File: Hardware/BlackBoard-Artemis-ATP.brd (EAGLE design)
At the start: 101.6 x 53.3 mm, 149 parts, among them IC3 LM1117, J2 CORTEX_DEBUG, J3 POWER_JACKTOE, J5 USB-C, Q1 1.1A/60V/600mΩ, U3 AP2112-3.3V, U4 ARTEMIS_MODULESMD, U5 CH340C, Y1 32.768kHz

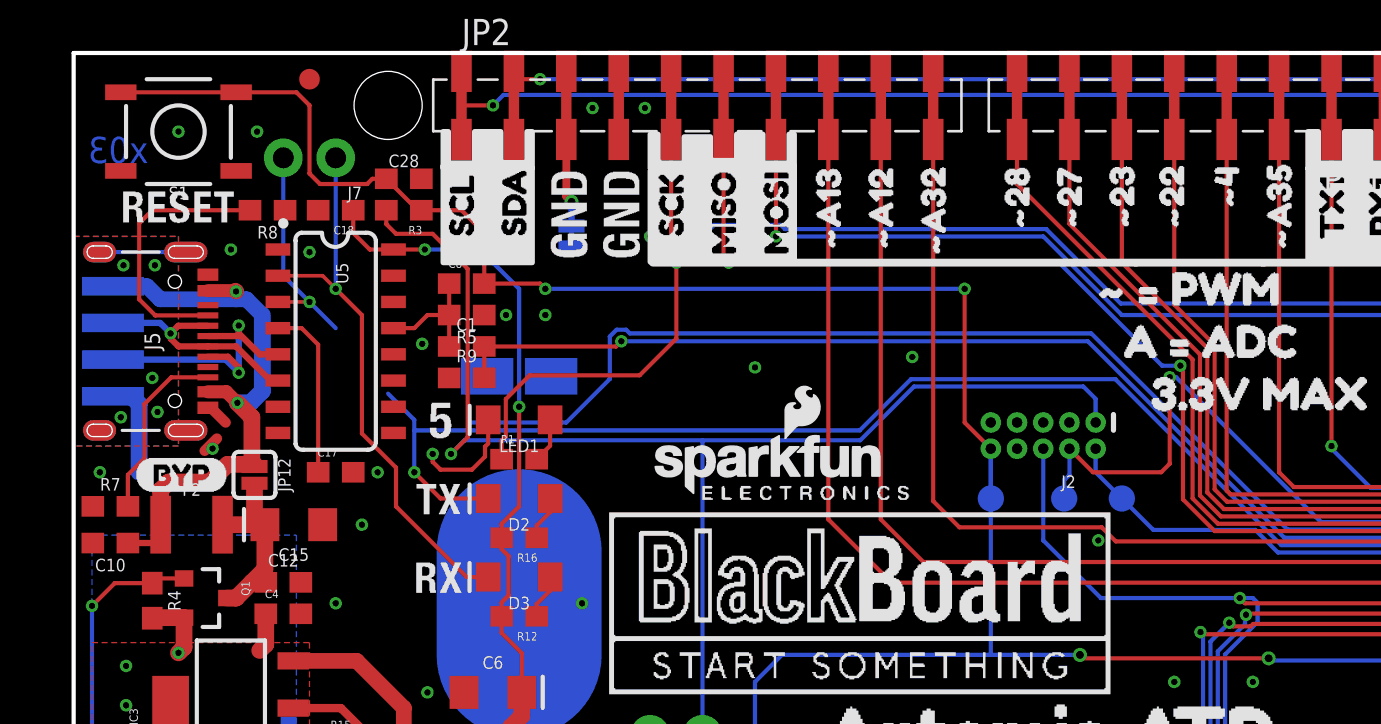
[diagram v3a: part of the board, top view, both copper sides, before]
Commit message: Move TP for easier testing. Remove TP on serial. Adjust sch blocks.
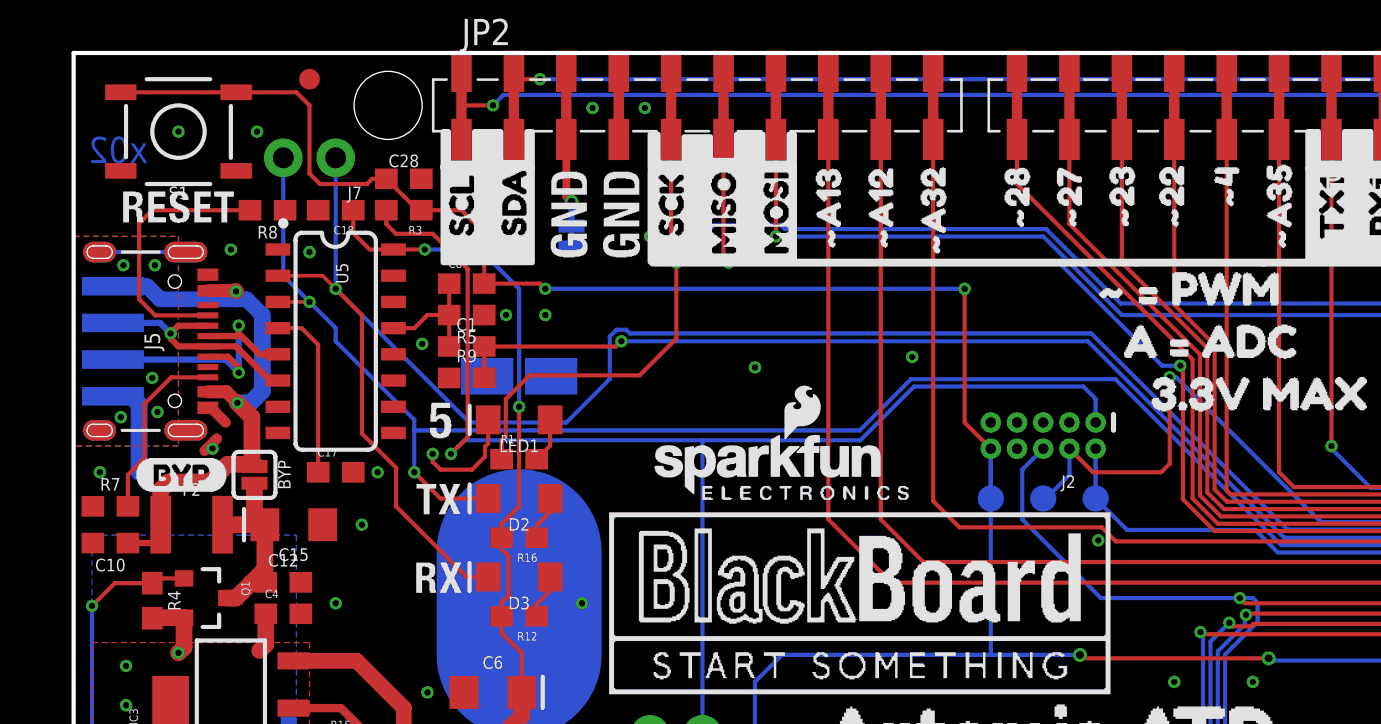
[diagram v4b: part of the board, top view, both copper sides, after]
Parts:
- BYP: value (none) -> BYP
- moved TP2 1.27 mm to (49.5, 31.8)
- moved TP1 1.02 mm to (47.0, 31.8)
- renumbered JP12 to BYP
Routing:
- net RXI-0: track 121.2 -> 130.4 mm
- net TXO-0: track 105.3 -> 109.6 mm
- net ~AD33/SWO: track 75.1 -> 76.0 mm
- net SWDIO: track 51.2 -> 51.9 mm
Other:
- board text added: "x02"
- board text removed: "x03"
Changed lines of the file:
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@@
 <wire x1="99.06" y1="51.816" x2="99.06" y2="40.386" width="0.2032" layer="20"/>
 <text x="0" y="-0.0635" size="0.0254" layer="214" font="vector">D:/SmartProjects/Snc/a4_bn_logo2.bmp</text>
-<text x="2.159" y="48.641" size="1.27" layer="16" font="vector" ratio="20" rot="MR180" align="center">x03</text>
+<text x="2.159" y="48.641" size="1.27" layer="16" font="vector" ratio="20" rot="MR180" align="center">x02</text>
 <rectangle x1="0.635" y1="22.352" x2="2.032" y2="30.607" layer="43"/>
 <rectangle x1="5.715" y1="23.114" x2="7.366" y2="30.607" layer="43"/>
@@
 <element name="U$2" library="buzzard_labels (14)" package="D#3" value="" x="5.588" y="38.481" smashed="yes" rot="MR0"/>
 <element name="U$10" library="buzzard_labels (14)" package="D#4" value="" x="5.461" y="40.259" smashed="yes" rot="MR0"/>
-<element name="JP12" library="SparkFun-Jumpers" package="SMT-JUMPER_2_NO_SILK" value="" x="8.763" y="32.893" smashed="yes" rot="R270">
+<element name="BYP" library="SparkFun-Jumpers" package="SMT-JUMPER_2_NO_SILK" value="BYP" x="8.763" y="32.893" smashed="yes" rot="R270">
 <attribute name="NAME" x="9.906" y="32.893" size="0.6096" layer="25" font="vector" ratio="20" rot="R270" align="bottom-center"/>
 <attribute name="VALUE" x="7.62" y="32.893" size="0.6096" layer="27" font="vector" ratio="20" rot="R270" align="top-center"/>
@@
 <attribute name="VALUE" value="6V/2A" x="5.715" y="30.48" size="1.778" layer="27" display="off"/>
 </element>
-<element name="TP1" library="SparkFun-Connectors" package="PAD.03X.05" value="" x="48.006" y="31.75" smashed="yes" rot="MR90"/>
-<element name="TP2" library="SparkFun-Connectors" package="PAD.03X.05" value="" x="50.8" y="31.75" smashed="yes" rot="MR90"/>
+<element name="TP1" library="SparkFun-Connectors" package="PAD.03X.05" value="" x="46.99" y="31.75" smashed="yes" rot="MR90"/>
+<element name="TP2" library="SparkFun-Connectors" package="PAD.03X.05" value="" x="49.53" y="31.75" smashed="yes" rot="MR90"/>
 <element name="J2" library="SparkFun-Connectors" package="2X5-PTH-1.27MM-NO_SILK" value="CORTEX_DEBUG" x="46.99" y="34.798" smashed="yes" rot="R180">
 <attribute name="NAME" x="48.5648" y="32.8676" size="0.6096" layer="25" font="vector" ratio="20" rot="R180"/>
@@
 <wire x1="19.05" y1="27.94" x2="20.09" y2="27.94" width="0.2032" layer="1"/>
 <wire x1="23.876" y1="35.433" x2="19.177" y2="35.433" width="0.2032" layer="16"/>
+<wire x1="19.177" y1="35.433" x2="13.97" y2="40.64" width="0.2032" layer="16"/>
 <contactref element="J7" pad="1"/>
 <wire x1="12.7" y1="48.26" x2="12.7" y2="41.91" width="0.2032" layer="16"/>
+<wire x1="12.7" y1="41.91" x2="13.97" y2="40.64" width="0.2032" layer="16"/>
 <contactref element="U4" pad="RXI-0"/>
 <via x="90.9444" y="37.13" extent="1-16" drill="0.3048"/>
@@
 <wire x1="25.9842" y1="39.60146875" x2="25.9842" y2="37.5412" width="0.2032" layer="16"/>
 <wire x1="49.3131" y1="39.751" x2="26.95226875" y2="39.751" width="0.2032" layer="16"/>
-<wire x1="15.624" y1="33.2442125" x2="19.177" y2="35.433" width="0" layer="19" extent="1-16"/>
 </signal>
 <signal name="TXO-0">
@@
 <wire x1="16.51" y1="35.052" x2="16.51" y2="33.02" width="0.2032" layer="16"/>
 <wire x1="11.43" y1="41.275" x2="12.7" y2="40.005" width="0.2032" layer="16"/>
+<wire x1="12.7" y1="40.005" x2="12.7" y2="39.37" width="0.2032" layer="16"/>
 <wire x1="40.57905" y1="37.53105" x2="38.1" y2="35.052" width="0.2032" layer="16"/>
 <wire x1="38.1" y1="35.052" x2="16.51" y2="35.052" width="0.2032" layer="16"/>
-<wire x1="15.24" y1="36.83" x2="16.51" y2="35.56" width="0.2032" layer="16"/>
+<wire x1="12.7" y1="39.37" x2="16.51" y2="35.56" width="0.2032" layer="16"/>
 <wire x1="16.51" y1="35.56" x2="16.51" y2="35.052" width="0.2032" layer="16"/>
 <contactref element="J7" pad="2"/>
@@
 <wire x1="75.45043125" y1="29.4894" x2="58.5267" y2="29.4894" width="0.2032" layer="16"/>
 <wire x1="50.48505" y1="37.53105" x2="40.57905" y2="37.53105" width="0.2032" layer="16"/>
-<wire x1="15.24" y1="36.83" x2="12.7" y2="40.005" width="0" layer="19" extent="16-16"/>
 </signal>
 <signal name="~D7/MOSI">
@@
 <contactref element="C15" pad="+"/>
 <contactref element="C12" pad="1"/>
-<contactref element="JP12" pad="2"/>
+<contactref element="BYP" pad="2"/>
 <contactref element="F2" pad="2"/>
 <wire x1="7.215" y1="30.48" x2="9.268" y2="30.48" width="0.8128" layer="1"/>
@@
 <via x="7.9375" y="36.3855" extent="1-16" drill="0.3048"/>
 <contactref element="JP14" pad="VBUS"/>
-<contactref element="JP12" pad="1"/>
+<contactref element="BYP" pad="1"/>
 <contactref element="F2" pad="1"/>
 <wire x1="6.504" y1="36.92" x2="7.403" y2="36.92" width="0.635" layer="1"/>
@@
 <contactref element="J2" pad="6"/>
 <via x="56.515" y="26.924" extent="1-16" drill="0.3048"/>
-<wire x1="49.784" y1="26.924" x2="46.99" y2="29.718" width="0.2032" layer="16"/>
-<wire x1="46.99" y1="29.718" x2="46.99" y2="34.163" width="0.2032" layer="16"/>
+<wire x1="49.784" y1="26.924" x2="45.974" y2="30.734" width="0.2032" layer="16"/>
+<wire x1="45.974" y1="33.147" x2="46.99" y2="34.163" width="0.2032" layer="16"/>
+<wire x1="45.974" y1="33.147" x2="45.974" y2="30.734" width="0.2032" layer="16"/>
 <wire x1="56.515" y1="26.924" x2="49.784" y2="26.924" width="0.2032" layer="16"/>
 <contactref element="U4" pad="~AD33/SWO"/>
@@
 <contactref element="TP2" pad="P$1"/>
 <contactref element="J2" pad="2"/>
-<wire x1="49.53" y1="34.163" x2="49.53" y2="33.02" width="0.2032" layer="16"/>
-<wire x1="50.8" y1="31.75" x2="49.53" y2="33.02" width="0.2032" layer="16"/>
+<wire x1="49.53" y1="34.163" x2="49.53" y2="31.75" width="0.2032" layer="16"/>
 <contactref element="U4" pad="SWDIO"/>
 <wire x1="93.599" y1="30.37" x2="93.599" y2="32.8248" width="0.2032" layer="1"/>
 <wire x1="93.599" y1="32.8248" x2="93.1498" y2="33.274" width="0.2032" layer="1"/>
 <via x="93.1498" y="33.274" extent="1-16" drill="0.3048"/>
-<wire x1="52.324" y1="30.226" x2="50.8" y2="31.75" width="0.2032" layer="16"/>
-<wire x1="57.2719" y1="30.226" x2="52.324" y2="30.226" width="0.2032" layer="16"/>
+<wire x1="51.054" y1="30.226" x2="49.53" y2="31.75" width="0.2032" layer="16"/>
+<wire x1="57.2719" y1="30.226" x2="51.054" y2="30.226" width="0.2032" layer="16"/>
 <wire x1="79.73793125" y1="33.274" x2="75.59773125" y2="29.1338" width="0.2032" layer="16"/>
 <wire x1="58.3641" y1="29.1338" x2="57.2719" y2="30.226" width="0.2032" layer="16"/>
@@
 <contactref element="J2" pad="4"/>
 <wire x1="48.26" y1="34.163" x2="48.26" y2="32.893" width="0.2032" layer="16"/>
-<wire x1="48.26" y1="32.893" x2="48.006" y2="32.639" width="0.2032" layer="16"/>
-<wire x1="48.006" y1="32.639" x2="48.006" y2="31.75" width="0.2032" layer="16"/>
+<wire x1="48.26" y1="32.893" x2="47.117" y2="31.75" width="0.2032" layer="16"/>
+<wire x1="47.117" y1="31.75" x2="46.99" y2="31.75" width="0.2032" layer="16"/>
 <contactref element="U4" pad="SWDCK"/>
 <wire x1="97.599" y1="33.86186875" x2="93.77206875" y2="37.6888" width="0.2032" layer="1"/>
